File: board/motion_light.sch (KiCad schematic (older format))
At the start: 20 parts, among them CON1 AVR-ISP-6, J1 MOTION, J2 Conn_01x05, J3 USB_MICRO, J4 USB_MICRO, Q1 BSS83P, Q2 BSS83P, SW1 SW_Push, SW2 SW_Push, U1 ATTINY84A-SSU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

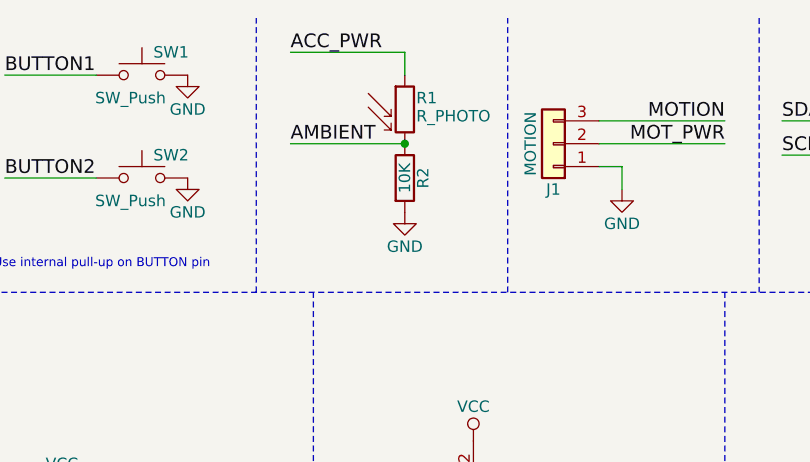
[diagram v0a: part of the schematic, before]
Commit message: Use 100K resistor for better ambient light sensitivity
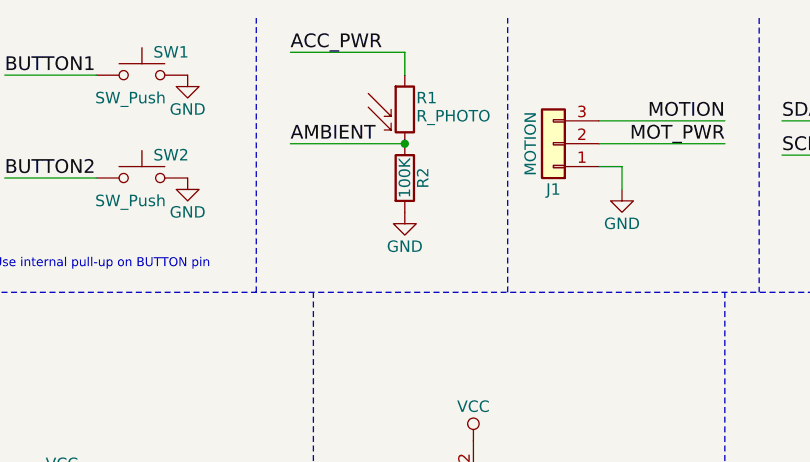
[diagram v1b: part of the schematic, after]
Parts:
- R2: value 10K -> 100K
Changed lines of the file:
@@
 P 6800 1200
 F 0 "R2" V 6880 1200 50  0000 C CNN
-F 1 "10K" V 6800 1200 50  0000 C CNN
+F 1 "100K" V 6800 1200 50  0000 C CNN
 F 2 "Resistor_SMD:R_0805_2012Metric_Pad1.15x1.40mm_HandSolder" V 6730 1200 50  0001 C CNN
 F 3 "" H 6800 1200 50  0001 C CNN

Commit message: Update to KiCAD 5.1
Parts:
- U2, U3: symbol crumpschemes:APA102 -> motion_light-rescue:APA102-crumpschemes
- U4: symbol steve_parts:PIR_MODULE -> motion_light-rescue:PIR_MODULE-steve_parts
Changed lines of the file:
@@
 EESchema Schematic File Version 4
 LIBS:motion_light-cache
-EELAYER 26 0
+EELAYER 30 0
 EELAYER END
 $Descr A4 11693 8268
@@
 $EndDescr
 $Comp
-L crumpschemes:APA102 U2
+L motion_light-rescue:APA102-crumpschemes U2
 U 1 1 59B43E23
 P 9200 1100
@@
 $EndComp
 $Comp
-L crumpschemes:APA102 U3
+L motion_light-rescue:APA102-crumpschemes U3
 U 1 1 59B43E3A
 P 10450 1100
@@
 $EndComp
 $Comp
-L steve_parts:PIR_MODULE U4
+L motion_light-rescue:PIR_MODULE-steve_parts U4
 U 1 1 59E6FCD5
 P 4050 2600
